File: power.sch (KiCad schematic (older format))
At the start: 49 parts, among them CN8 Power_Conn, U1 68000D, U10 74LS244, U11 74LS373, U12 74LS244, U13 74LS373, U2 FAT_AGNUS_8375, U32 74LS139, U34 74LS373, U35 74LS244, U36 74LS05, U37 74LS32, U5 GARY_5719, X1 XTAL

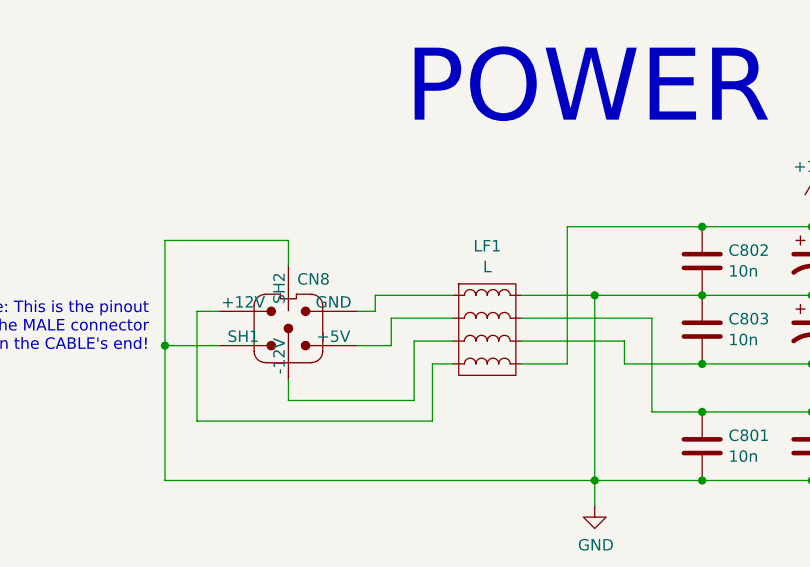
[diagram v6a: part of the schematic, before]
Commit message: Almost all components positioned
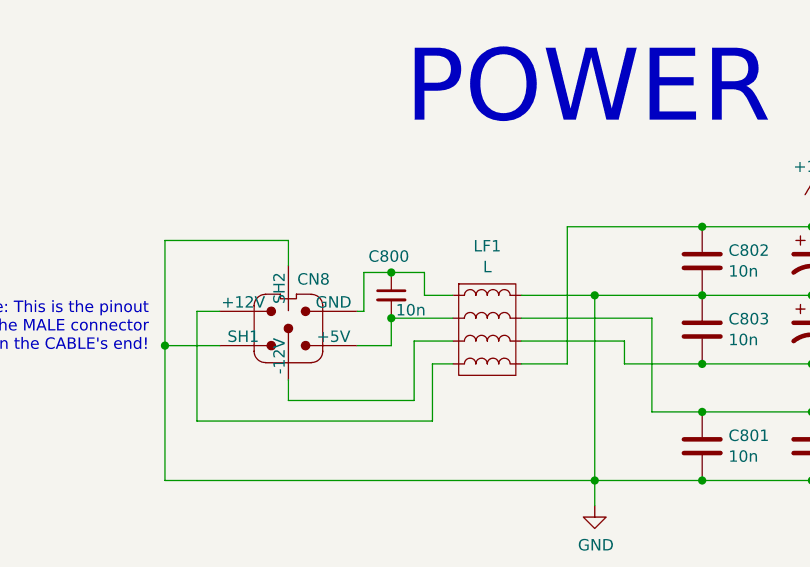
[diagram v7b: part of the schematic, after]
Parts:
- added C800: 10n, Raemixx500:C_Axial_L6.3mm_D2.5mm_P10.16mm, symbol Device:C_Small
- C701: footprint (none) -> Raemixx500:C_Axial_L6.3mm_D2.5mm_P10.16mm
- E101, E110: footprint (none) -> Raemixx500:EMI_Filter_Short
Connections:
- net at CN8.1 (+5V), LF1.2: now also C800.2
- net at CN8.4 (GND), LF1.1: now also C800.1
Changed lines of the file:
@@
 F 0 "E101" V 4274 4289 50  0000 L CNN
 F 1 "10n" V 4365 4289 50  0000 L CNN
-F 2 "" V 4320 4110 50  0001 C CNN
+F 2 "Raemixx500:EMI_Filter_Short" V 4320 4110 50  0001 C CNN
 F 3 "http://www.murata.com/~/media/webrenewal/support/library/catalog/products/emc/emifil/c31e.ashx?la=en-gb" V 4320 4110 50  0001 C CNN
 	1    4320 4110
@@
 F 0 "E110" V 5724 4289 50  0000 L CNN
 F 1 "10n" V 5815 4289 50  0000 L CNN
-F 2 "" V 5770 4110 50  0001 C CNN
+F 2 "Raemixx500:EMI_Filter_Short" V 5770 4110 50  0001 C CNN
 F 3 "http://www.murata.com/~/media/webrenewal/support/library/catalog/products/emc/emifil/c31e.ashx?la=en-gb" V 5770 4110 50  0001 C CNN
 	1    5770 4110
@@
 F 0 "C701" H 6385 5156 50  0000 L CNN
 F 1 "10n" H 6385 5065 50  0000 L CNN
-F 2 "" H 6308 4960 50  0001 C CNN
+F 2 "Raemixx500:C_Axial_L6.3mm_D2.5mm_P10.16mm" H 6308 4960 50  0001 C CNN
 F 3 "~" H 6270 5110 50  0001 C CNN
 	1    6270 5110
@@
 Text Notes 2210 2020 2    50   ~ 0
 Note: This is the pinout\nof the MALE connector\non the CABLE's end!
-Wire Wire Line
-	3120 1840 3200 1840
-Wire Wire Line
-	3200 1840 3200 1770
-Wire Wire Line
-	3200 1770 3540 1770
 Wire Wire Line
 	3120 1990 3270 1990
@@
 Text Notes 8090 9060 0    315  ~ 0
 GROUNDED\nHOLES
+$Comp
+L Device:C_Small C800
+U 1 1 5D4BE8BA
+P 3270 1770
+F 0 "C800" H 3170 1940 50  0000 L CNN
+F 1 "10n" H 3290 1705 50  0000 L CNN
+F 2 "Raemixx500:C_Axial_L6.3mm_D2.5mm_P10.16mm" H 3270 1770 50  0001 C CNN
+F 3 "~" H 3270 1770 50  0001 C CNN
+	1    3270 1770
+	1    0    0    -1
+$EndComp
+Connection ~ 3270 1870
+Wire Wire Line
+	3120 1840 3150 1840
+Wire Wire Line
+	3150 1840 3150 1670
+Wire Wire Line
+	3150 1670 3270 1670
+Wire Wire Line
+	3270 1670 3415 1670
+Wire Wire Line
+	3415 1670 3415 1770
+Wire Wire Line
+	3415 1770 3540 1770
+Connection ~ 3270 1670
 $EndSCHEMATC

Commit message: Work in progress
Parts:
- LF1: footprint (none) -> Raemixx500:LineFilter
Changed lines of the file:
@@
 F 0 "LF1" H 3690 2285 50  0000 C CNN
 F 1 "L" H 3690 2194 50  0000 C CNN
-F 2 "" V 3690 1970 50  0001 C CNN
+F 2 "Raemixx500:LineFilter" V 3690 1970 50  0001 C CNN
 F 3 "~" V 3690 1970 50  0001 C CNN
 	1    3690 1920
